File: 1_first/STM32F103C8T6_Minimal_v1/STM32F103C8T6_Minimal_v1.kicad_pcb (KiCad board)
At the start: 2 copper layers, 35 parts, among them J1 Conn_01x06, J2 USB_B_Micro, SW1 SW_SPDT, SW2 SW_Push, SW3 SW_Push, U1 AMS1117-3.3, U2 STM32F103C8Tx, Y1 8MHz

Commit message: pcb updated
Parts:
- moved J1 144.2 mm to (112.5, 93.3)
- moved SW1 143.8 mm to (112.5, 82.2)
- moved SW3 139.3 mm to (111.0, 124.5)
- moved SW2 138.8 mm to (111.8, 114.2)
- moved J2 120.7 mm to (171.4, 98.3), turned to -90 degrees
- moved D1 113.8 mm to (171.5, 90.0)
- moved C1 102.1 mm to (170.0, 80.5), turned to 90 degrees
- moved D2 96.8 mm to (151.0, 84.5), turned to 90 degrees
- moved R1 96.8 mm to (151.0, 89.0), turned to -90 degrees
- moved C2 96.1 mm to (166.0, 91.5)
- moved R8 95.7 mm to (150.0, 95.0), turned to -90 degrees
- moved C3 95.2 mm to (161.5, 78.0)
- moved U1 84.7 mm to (159.5, 86.5), turned to 90 degrees
- moved C4 82.4 mm to (152.0, 78.0)
- moved R2 6.52 mm to (137.0, 84.5)
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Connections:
- C1 pad 2: +3.3V -> GND
- C10 pad 2: +3.3V -> GND
- C11 pad 2: +3.3V -> GND
- C12 pad 2: +3.3V -> GND
- C13 pad 2: +3.3V -> GND
- C14 pad 2: +3.3V -> GND
- C15 pad 2: +3.3V -> GND
- C2 pad 2: +3.3V -> GND
- C3 pad 2: +3.3V -> GND
- C4 pad 2: +3.3V -> GND
- C5 pad 2: +3.3V -> GND
- C6 pad 2: +3.3V -> GND
- C7 pad 2: +3.3V -> GND
- C8 pad 2: +3.3V -> GND
- C9 pad 2: +3.3V -> GND
- J1 pad 3: +3.3V -> GND
- J1 pad 5: +3.3V -> GND
- J2 pad 5: +3.3V -> GND
- J2 pad SH: +3.3V -> GND
- R1 pad 2: +3.3V -> GND
- R5 pad 1: +3.3V -> GND
- SW1 pad 1: +3.3V -> GND
- SW2 pad 2: +3.3V -> GND
- U1 pad 1: +3.3V -> GND
- U2 pad 23: +3.3V -> GND
- U2 pad 35: +3.3V -> GND
- U2 pad 47: +3.3V -> GND
- U2 pad 8: +3.3V -> GND
- Y1 pad 2: +3.3V -> GND
- Y1 pad 4: +3.3V -> GND
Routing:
- net GND: track 0.00 -> 152.3 mm
- net +3.3V: track 0.00 -> 64.8 mm
- net Net-(U2-PA0): track 0.00 -> 45.1 mm
- net /MCU/NRST: track 0.00 -> 33.6 mm
- net Net-(J2-D-): track 0.00 -> 29.6 mm
- net Net-(J2-D+): track 0.00 -> 27.7 mm
- net Net-(SW1-B): track 0.00 -> 25.4 mm
- net Net-(D1-K): track 0.00 -> 16.8 mm
- net /MCU/HSE_OUT: track 0.00 -> 13.2 mm
- net Net-(U2-BOOT0): track 0.00 -> 12.5 mm
- net PA12: track 0.00 -> 9.26 mm
- net VBUS: track 0.00 -> 8.37 mm
- net PA11: track 0.00 -> 6.54 mm
- net /MCU/HSE_IN: track 0.00 -> 6.41 mm
- net Net-(D2-K): track 0.00 -> 2.62 mm

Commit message: Reroute
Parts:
- added U3: USBLC6-2SC6, Package_TO_SOT_SMD:SOT-23-6, F.Cu at (27.8, 139.1)
- moved C3 135.9 mm to (28.5, 106.0)
- moved C1 131.8 mm to (39.0, 95.0), turned to 0 degrees
- moved D1 129.3 mm to (43.0, 104.5)
- moved D2 126.3 mm to (29.4, 118.5), turned to 0 degrees
- moved U1 120.8 mm to (46.0, 45.0), turned to 0 degrees
- moved J2 111.8 mm to (62.4, 123.1), turned to 0 degrees
- moved C2 109.0 mm to (59.8, 115.9)
- moved C4 100.9 mm to (59.8, 118.9)
- moved R1 97.8 mm to (55.0, 107.5), turned to 0 degrees
- moved R8 97.4 mm to (55.0, 116.4), turned to 0 degrees
- moved R6 96.8 mm to (55.0, 110.5), turned to 0 degrees
- moved R7 95.9 mm to (55.0, 113.5), turned to 0 degrees
- moved D3 91.0 mm to (50.7, 100.5)
- moved J1 85.3 mm to (197.5, 100.3)
- moved R4 77.2 mm to (124.5, 43.5)
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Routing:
- net GND: track 152.3 -> 0.00 mm
- net +3.3V: track 64.8 -> 0.00 mm
- net Net-(U2-PA0): track 45.1 -> 0.00 mm
- net /MCU/NRST: track 33.6 -> 0.00 mm
- net Net-(J2-D-): track 29.6 -> 0.00 mm
- net Net-(J2-D+): track 27.7 -> 0.00 mm
- net Net-(SW1-B): track 25.4 -> 0.00 mm
- net Net-(D1-K): track 16.8 -> 0.00 mm
- net /MCU/HSE_OUT: track 13.2 -> 0.00 mm
- net Net-(U2-BOOT0): track 12.5 -> 0.00 mm
- net PA12: track 9.26 -> 0.00 mm
- net VBUS: track 8.37 -> 0.00 mm
- net PA11: track 6.54 -> 0.00 mm
- net /MCU/HSE_IN: track 6.41 -> 0.00 mm
- net Net-(D2-K): track 2.62 -> 0.00 mm
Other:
- copper layers 2 -> 4

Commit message: grouped parts
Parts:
- removed R6, R7: 22, Resistor_SMD:R_0805_2012Metric_Pad1.20x1.40mm_HandSolder
- moved U3 149.2 mm to (170.0, 94.0), turned to 180 degrees
- moved U1 146.1 mm to (174.0, 115.5), turned to 90 degrees
- moved C3 145.0 mm to (173.5, 104.5), turned to 180 degrees
- moved D1 141.5 mm to (184.0, 117.0), turned to 90 degrees
- moved C1 138.9 mm to (174.2, 127.0), turned to 180 degrees
- moved D2 129.3 mm to (158.6, 115.0)
- moved J2 124.2 mm to (183.2, 94.1), turned to -90 degrees
- moved C2 115.1 mm to (173.5, 134.0), turned to 180 degrees
- moved R1 105.8 mm to (159.0, 127.0)
- moved C13 105.0 mm to (113.5, 128.0), turned to -90 degrees
- moved C4 101.7 mm to (160.5, 105.0)
- moved R8 93.9 mm to (146.5, 95.5)
- moved R3 79.0 mm to (125.5, 119.5), turned to 90 degrees
- moved R5 73.2 mm to (134.0, 119.0)
- moved D3 67.3 mm to (116.1, 84.5)
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
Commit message: grouped closely
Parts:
- moved D1 30.7 mm to (154.0, 110.5)
- moved J2 30.7 mm to (153.2, 87.6)
- moved C2 28.6 mm to (146.5, 124.5)
- moved C1 28.5 mm to (146.7, 119.5)
- moved J1 28.4 mm to (146.1, 77.0)
- moved C3 28.1 mm to (146.0, 98.5)
- moved U1 28.1 mm to (146.5, 109.5)
- moved U3 28.1 mm to (142.5, 88.0)
- moved R1 22.8 mm to (137.5, 119.5)
- moved C4 22.3 mm to (139.0, 99.0)
- moved D2 22.3 mm to (137.1, 109.0)
- moved SW1 18.5 mm to (121.5, 76.2)
- moved C13 13.1 mm to (104.8, 118.2)
- moved SW2 13.1 mm to (110.5, 116.0)
- moved SW3 13.1 mm to (122.5, 116.0)
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
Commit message: Board cut
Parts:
- moved D1 10.5 mm to (154.0, 100.0)
- moved U1 10.2 mm to (148.5, 99.5)
- moved C1 10.0 mm to (147.0, 109.5)
- moved C2 10.0 mm to (146.8, 114.5)
- moved R1 8.56 mm to (138.5, 111.0)
- moved SW1 7.81 mm to (126.5, 82.2)
- moved C3 7.02 mm to (139.0, 98.0)
- moved C4 7.02 mm to (132.0, 98.5)
- moved D3 4.39 mm to (115.1, 81.5)
- moved R4 4.39 mm to (119.6, 81.5)
- moved J1 4.20 mm to (147.3, 81.0)
- moved D2 3.76 mm to (138.5, 105.5)
- moved C13 2.75 mm to (104.8, 115.5)
- moved SW2 2.75 mm to (110.5, 113.2)
- moved SW3 2.75 mm to (122.5, 113.2)
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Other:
- board outline added: 54 x 41 mm
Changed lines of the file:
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@@
 	(footprint "Capacitor_SMD:CP_Elec_5x5.3"
 		(layer "F.Cu")
-		(at 146.7 119.5 180)
+		(at 147 109.5 180)
 		(descr "SMD capacitor, aluminum electrolytic, Nichicon, 5.0x5.3mm")
 		(tags "capacitor electrolytic")
 		(property "Reference" "C1"
-			(at -5.8 -0.5 0)
+			(at -5 -2.5 0)
 			(layer "F.SilkS")
 			(effects
@@
 	(footprint "Connector_PinHeader_2.54mm:PinHeader_1x06_P2.54mm_Vertical"
 		(layer "F.Cu")
-		(at 146.08 77 -90)
+		(at 147.35 81 -90)
 		(descr "Through hole straight pin header, 1x06, 2.54mm pitch, single row")
 		(tags "Through hole pin header THT 1x06 2.54mm single row")
@@
 		)
 		(property "Value" "Conn_01x06"
-			(at 0 15.08 90)
+			(at 2.35 7.4 180)
 			(layer "F.Fab")
 			(effects
@@
 	(footprint "Capacitor_SMD:CP_Elec_5x5.3"
 		(layer "F.Cu")
-		(at 146 98.5 180)
+		(at 139 98 180)
 		(descr "SMD capacitor, aluminum electrolytic, Nichicon, 5.0x5.3mm")
 		(tags "capacitor electrolytic")
@@
 	(footprint "Button_Switch_THT:SW_PUSH_6mm_H5mm"
 		(layer "F.Cu")
-		(at 122.5 116)
+		(at 122.5 113.25)
 		(descr "tactile push button, 6x6mm e.g. PHAP33xx series, height=5mm")
 		(tags "tact sw push 6mm")
@@
 		)
 		(property "Value" "SW_Push"
-			(at 3.75 6.7 0)
+			(at 11.35 2.5 0)
 			(layer "F.Fab")
 			(effects
@@
 	(footprint "Button_Switch_THT:SW_PUSH_6mm_H5mm"
 		(layer "F.Cu")
-		(at 110.5 116)
+		(at 110.5 113.25)
 		(descr "tactile push button, 6x6mm e.g. PHAP33xx series, height=5mm")
 		(tags "tact sw push 6mm")
@@
 		)
 		(property "Value" "SW_Push"
-			(at 3.75 6.7 0)
+			(at -4.75 5.45 0)
 			(layer "F.Fab")
 			(effects
@@
 	(footprint "Resistor_SMD:R_0805_2012Metric_Pad1.20x1.40mm_HandSolder"
 		(layer "F.Cu")
-		(at 115.5 80)
+		(at 119.625 81.5)
 		(descr "Resistor SMD 0805 (2012 Metric), square (rectangular) end terminal, IPC-7351 nominal with elongated pad for handsoldering. (Body size source: IPC-SM-782 page 72, https://www.pcb-3d.com/wordpress/wp-content/uploads/ipc-sm-782a_amendment_1_and_2.pdf)")
 		(tags "resistor handsolder")
@@
 	(footprint "Resistor_SMD:R_0805_2012Metric_Pad1.20x1.40mm_HandSolder"
 		(layer "F.Cu")
-		(at 120.5 83.5 -90)
+		(at 121 86 -90)
 		(descr "Resistor SMD 0805 (2012 Metric), square (rectangular) end terminal, IPC-7351 nominal with elongated pad for handsoldering. (Body size source: IPC-SM-782 page 72, https://www.pcb-3d.com/wordpress/wp-content/uploads/ipc-sm-782a_amendment_1_and_2.pdf)")
 		(tags "resistor handsolder")
@@
 	(footprint "LED_SMD:LED_0603_1608Metric_Pad1.05x0.95mm_HandSolder"
 		(layer "F.Cu")
-		(at 111 80)
+		(at 115.125 81.5)
 		(descr "LED SMD 0603 (1608 Metric), square (rectangular) end terminal, IPC-7351 nominal, (Body size source: http://www.tortai-tech.com/upload/download/2011102023233369053.pdf)")
 		(tags "LED handsolder")
@@
 	(footprint "Resistor_SMD:R_0805_2012Metric_Pad1.20x1.40mm_HandSolder"
 		(layer "F.Cu")
-		(at 125 109.5)
+		(at 125 107.5)
 		(descr "Resistor SMD 0805 (2012 Metric), square (rectangular) end terminal, IPC-7351 nominal with elongated pad for handsoldering. (Body size source: IPC-SM-782 page 72, https://www.pcb-3d.com/wordpress/wp-content/uploads/ipc-sm-782a_amendment_1_and_2.pdf)")
 		(tags "resistor handsolder")
@@
 	(footprint "LED_SMD:LED_0603_1608Metric_Pad1.05x0.95mm_HandSolder"
 		(layer "F.Cu")
-		(at 137.125 109)
+		(at 138.5 105.5)
 		(descr "LED SMD 0603 (1608 Metric), square (rectangular) end terminal, IPC-7351 nominal, (Body size source: http://www.tortai-tech.com/upload/download/2011102023233369053.pdf)")
 		(tags "LED handsolder")
@@
 	(footprint "Diode_SMD:D_SOD-123"
 		(layer "F.Cu")
-		(at 154 110.5 90)
+		(at 154 100 90)
 		(descr "SOD-123")
 		(tags "SOD-123")
 		(property "Reference" "D1"
-			(at 0 -2 90)
+			(at 3.5 0 90)
 			(layer "F.SilkS")
 			(effects
@@
 		)
 		(property "Value" "D_Schottky"
-			(at 0 2.1 90)
+			(at -6.5 0 270)
 			(layer "F.Fab")
 			(effects
@@
 		)
 		(fp_text user "${REFERENCE}"
-			(at 0 -2 90)
+			(at 3.5 0 90)
 			(layer "F.Fab")
 			(effects
@@
 	(footprint "Capacitor_SMD:C_0805_2012Metric_Pad1.18x1.45mm_HandSolder"
 		(layer "F.Cu")
-		(at 118 87)
+		(at 117.5 87)
 		(descr "Capacitor SMD 0805 (2012 Metric), square (rectangular) end terminal, IPC-7351 nominal with elongated pad for handsoldering. (Body size source: IPC-SM-782 page 76, https://www.pcb-3d.com/wordpress/wp-content/uploads/ipc-sm-782a_amendment_1_and_2.pdf, https://docs.google.com/spreadsheets/d/1BsfQQcO9C6DZCsRaXUlFlo91Tg2WpOkGARC1WS5S8t0/edit?usp=sharing)")
 		(tags "capacitor handsolder")
@@
 	(footprint "Package_TO_SOT_SMD:SOT-223-3_TabPin2"
 		(layer "F.Cu")
-		(at 146.5 109.5 90)
+		(at 148.5 99.5 90)
 		(descr "module CMS SOT223 4 pins")
 		(tags "CMS SOT")
@@
 		)
 		(property "Value" "AMS1117-3.3"
-			(at 0 4.5 90)
+			(at 5.5 0 180)
 			(layer "F.Fab")
 			(effects
@@
 	(footprint "Button_Switch_SMD:SW_SPDT_PCM12"
 		(layer "F.Cu")
-		(at 121.5 76.17)
+		(at 126.5 82.17)
 		(descr "Ultraminiature Surface Mount Slide Switch, right-angle, https://www.ckswitches.com/media/1424/pcm.pdf")
 		(property "Reference" "SW1"
-			(at 0 -3.2 0)
+			(at 3.75 2.98 0)
 			(layer "F.SilkS")
 			(effects
@@
 		)
 		(fp_text user "${REFERENCE}"
-			(at 0 -3.2 0)
+			(at 3.75 2.98 0)
 			(layer "F.Fab")
 			(effects
@@
 	(footprint "Capacitor_SMD:C_0805_2012Metric_Pad1.18x1.45mm_HandSolder"
 		(layer "F.Cu")
-		(at 104.75 118.25 -90)
+		(at 104.75 115.5 -90)
 		(descr "Capacitor SMD 0805 (2012 Metric), square (rectangular) end terminal, IPC-7351 nominal with elongated pad for handsoldering. (Body size source: IPC-SM-782 page 76, https://www.pcb-3d.com/wordpress/wp-content/uploads/ipc-sm-782a_amendment_1_and_2.pdf, https://docs.google.com/spreadsheets/d/1BsfQQcO9C6DZCsRaXUlFlo91Tg2WpOkGARC1WS5S8t0/edit?usp=sharing)")
 		(tags "capacitor handsolder")
@@
 	(footprint "Capacitor_SMD:C_0805_2012Metric_Pad1.18x1.45mm_HandSolder"
 		(layer "F.Cu")
-		(at 146.5 124.5 180)
+		(at 146.8 114.5 180)
 		(descr "Capacitor SMD 0805 (2012 Metric), square (rectangular) end terminal, IPC-7351 nominal with elongated pad for handsoldering. (Body size source: IPC-SM-782 page 76, https://www.pcb-3d.com/wordpress/wp-content/uploads/ipc-sm-782a_amendment_1_and_2.pdf, https://docs.google.com/spreadsheets/d/1BsfQQcO9C6DZCsRaXUlFlo91Tg2WpOkGARC1WS5S8t0/edit?usp=sharing)")
 		(tags "capacitor handsolder")
@@
 	(footprint "Resistor_SMD:R_0805_2012Metric_Pad1.20x1.40mm_HandSolder"
 		(layer "F.Cu")
-		(at 116.5 110 90)
+		(at 116.5 108 90)
 		(descr "Resistor SMD 0805 (2012 Metric), square (rectangular) end terminal, IPC-7351 nominal with elongated pad for handsoldering. (Body size source: IPC-SM-782 page 72, https://www.pcb-3d.com/wordpress/wp-content/uploads/ipc-sm-782a_amendment_1_and_2.pdf)")
 		(tags "resistor handsolder")
@@
 		(tags "capacitor handsolder")
 		(property "Reference" "C15"
-			(at 0 -1.43 90)
+			(at -3.4 0.05 90)
 			(layer "F.SilkS")
 			(effects
@@
 	(footprint "Capacitor_SMD:C_0805_2012Metric_Pad1.18x1.45mm_HandSolder"
 		(layer "F.Cu")
-		(at 139 99)
+		(at 132 98.5)
 		(descr "Capacitor SMD 0805 (2012 Metric), square (rectangular) end terminal, IPC-7351 nominal with elongated pad for handsoldering. (Body size source: IPC-SM-782 page 76, https://www.pcb-3d.com/wordpress/wp-content/uploads/ipc-sm-782a_amendment_1_and_2.pdf, https://docs.google.com/spreadsheets/d/1BsfQQcO9C6DZCsRaXUlFlo91Tg2WpOkGARC1WS5S8t0/edit?usp=sharing)")
 		(tags "capacitor handsolder")
@@
 	(footprint "Resistor_SMD:R_0805_2012Metric_Pad1.20x1.40mm_HandSolder"
 		(layer "F.Cu")
-		(at 137.5 119.5)
+		(at 138.5 111)
 		(descr "Resistor SMD 0805 (2012 Metric), square (rectangular) end terminal, IPC-7351 nominal with elongated pad for handsoldering. (Body size source: IPC-SM-782 page 72, https://www.pcb-3d.com/wordpress/wp-content/uploads/ipc-sm-782a_amendment_1_and_2.pdf)")
 		(tags "resistor handsolder")
@@
 		(tags "Micro-USB SMD Typ-B Vertical")
 		(property "Reference" "J2"
-			(at 0 -2.85 90)
+			(at -5.125 0.1 90)
 			(layer "F.SilkS")
 			(effects
@@
 		)
 	)
+	(gr_line
+		(start 102 120)
+		(end 102 79)
+		(stroke
+			(width 0.05)
+			(type default)
+		)
+		(layer "Edge.Cuts")
+	)
+	(gr_line
+		(start 102 120)
+		(end 156 120)
+		(stroke
+			(width 0.05)
+			(type default)
+		)
+		(layer "Edge.Cuts")
+	)
+	(gr_line
+		(start 156 79)
+		(end 102 79)
+		(stroke
+			(width 0.05)
+			(type default)
+		)
+		(layer "Edge.Cuts")
+	)
+	(gr_line
+		(start 156 120)
+		(end 156 79)
+		(stroke
+			(width 0.05)
+			(type default)
+		)
+		(layer "Edge.Cuts")
+	)
 	(embedded_fonts no)

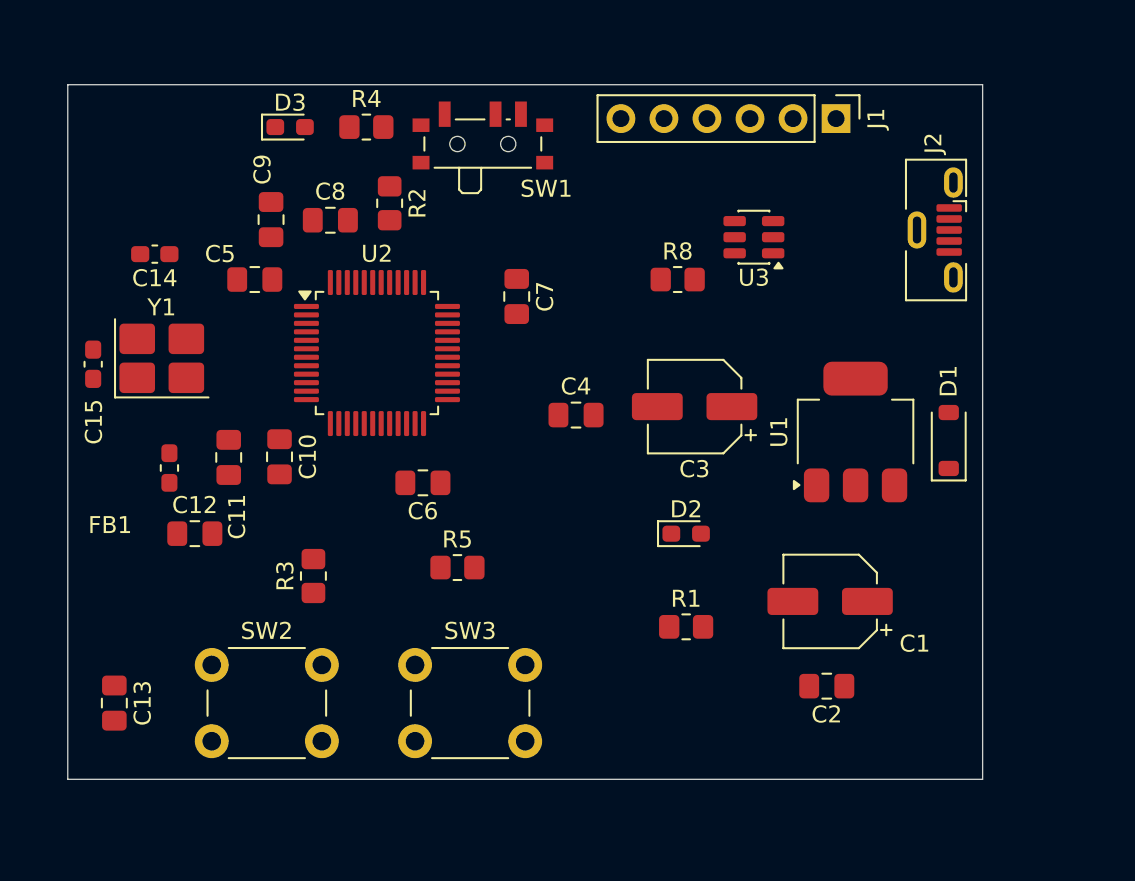
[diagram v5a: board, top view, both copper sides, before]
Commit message: copper fill
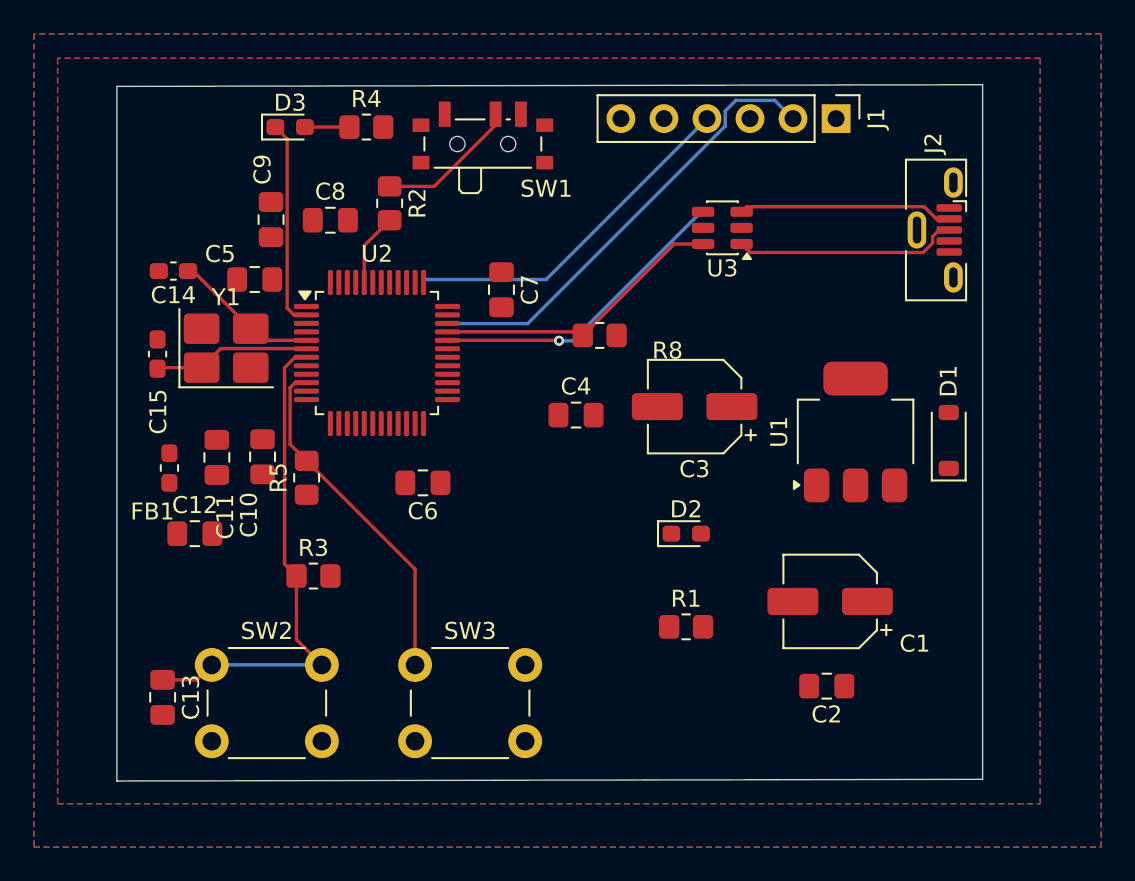
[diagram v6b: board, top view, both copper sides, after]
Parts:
- moved R5 10.4 mm to (116.1, 102.2), turned to 90 degrees
- moved R8 5.66 mm to (133.4, 93.8), turned to 180 degrees
- moved Y1 3.85 mm to (111.3, 94.5)
- moved C15 3.85 mm to (107.3, 94.9)
- moved C13 2.87 mm to (107.6, 115.2)
- moved U3 1.94 mm to (140.6, 87.5)
- moved C14 1.49 mm to (108.2, 90.0)
- moved C10 1.00 mm to (113.5, 101.0)
- moved C7 0.98 mm to (127.6, 91.1)
- moved C11 0.70 mm to (110.8, 101.0)
- turned R3 to 0 degrees
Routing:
- net /MCU/NRST: track 0.00 -> 29.8 mm
- net /MCU/SWDIO: track 0.00 -> 26.8 mm
- net /MCU/SWCLK: track 0.00 -> 20.7 mm
- net Net-(U2-PA0): track 0.00 -> 20.5 mm
- net PA11: track 0.00 -> 18.2 mm, vias 0 -> 1
- net PA12: track 0.00 -> 17.4 mm
- net Net-(J2-D+): track 0.00 -> 13.2 mm
- net Net-(J2-D-): track 0.00 -> 12.7 mm
- net Net-(D3-K): track 0.00 -> 12.3 mm
- net /MCU/HSE_OUT: track 0.00 -> 9.29 mm
- net /MCU/HSE_IN: track 0.00 -> 8.68 mm
- net Net-(SW1-B): track 0.00 -> 8.39 mm
- net Net-(U2-BOOT0): track 0.00 -> 4.30 mm
- net Net-(D3-A): track 0.00 -> 2.62 mm
- added copper zone on B.Cu, net GND
- added copper zone on F.Cu, net GND
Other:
- board size 54 x 41 mm -> 51.1 x 41.1 mm
- copper layers 4 -> 2

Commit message: connected parts
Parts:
- moved U3 7.80 mm to (148.4, 87.3)
- moved J1 2.61 mm to (144.7, 81.1)
- moved R4 1.57 mm to (118.5, 82.6), turned to -90 degrees
- moved SW1 1.52 mm to (125.0, 82.4)
- moved R2 0.98 mm to (120.6, 86.9)
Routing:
- net +3.3V: track 0.00 -> 130.2 mm
- net /MCU/NRST: track 29.8 -> 51.7 mm, vias 0 -> 2
- net VBUS: track 0.00 -> 21.4 mm
- net Net-(D1-K): track 0.00 -> 16.7 mm
- net +3.3VA: track 0.00 -> 11.1 mm
- net PA12: track 17.4 -> 25.3 mm, vias 0 -> 1
- net Net-(J2-D-): track 12.7 -> 4.77 mm
- net PA11: track 18.2 -> 25.9 mm
- net Net-(J2-D+): track 13.2 -> 5.59 mm
- net Net-(U2-PA0): track 20.5 -> 26.9 mm, vias 0 -> 1
- net Net-(D2-K): track 0.00 -> 5.83 mm
- net /MCU/SWDIO: track 26.8 -> 23.6 mm, vias 0 -> 1
- net /MCU/SWCLK: track 20.7 -> 18.1 mm
- net Net-(U2-BOOT0): track 4.30 -> 3.23 mm
- net Net-(SW1-B): track 8.39 -> 7.74 mm
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
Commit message: fixing routes
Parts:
- moved U3 26.3 mm to (140.5, 112.3), turned to 0 degrees
- moved J2 25.8 mm to (152.4, 113.4)
- moved C2 16.5 mm to (148.9, 98.1)
- moved C4 9.10 mm to (140.9, 96.6), turned to 180 degrees
- moved U1 8.88 mm to (150.3, 90.8)
- moved C3 8.79 mm to (140.8, 89.4)
- moved C1 5.41 mm to (146.7, 104.1)
- moved R1 4.79 mm to (140.4, 106.6)
- moved D2 4.38 mm to (140.5, 101.6)
- moved D1 0.82 mm to (153.2, 99.8), turned to -90 degrees
- moved R8 0.10 mm to (133.4, 93.7)
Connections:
- U3 pad 1: Net-(J2-D+) -> PA12
- U3 pad 3: Net-(J2-D-) -> PA11
- U3 pad 4: PA11 -> Net-(J2-D-)
- U3 pad 6: PA12 -> Net-(J2-D+)
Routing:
- net PA11: track 25.9 -> 0.00 mm, vias 1 -> 0
- net PA12: track 25.3 -> 0.00 mm, vias 1 -> 0
- net Net-(J2-D-): track 4.77 -> 13.6 mm
- net Net-(J2-D+): track 5.59 -> 12.9 mm, vias 0 -> 1
- net Net-(D2-K): track 5.83 -> 0.00 mm
- net Net-(D1-K): track 16.7 -> 14.2 mm
- net VBUS: track 21.4 -> 23.6 mm
- net GND: track 0.00 -> 0.64 mm
- net +3.3V: track 130.2 -> 129.6 mm
